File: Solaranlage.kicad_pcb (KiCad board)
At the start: 2 copper layers, 180.3 x 85 mm, 111 parts, among them J1 Screw_Terminal_01x02, J2 Screw_Terminal_01x02, J3 AVR-JTAG-10, J4 USB_B, J5 USB_B, J6 Screw_Terminal_01x02, J7 Screw_Terminal_01x02, Q1 2N3904, SW1 Rotary_Encoder_Switch_Panason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, SW2 100SP1T1B4M2QE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

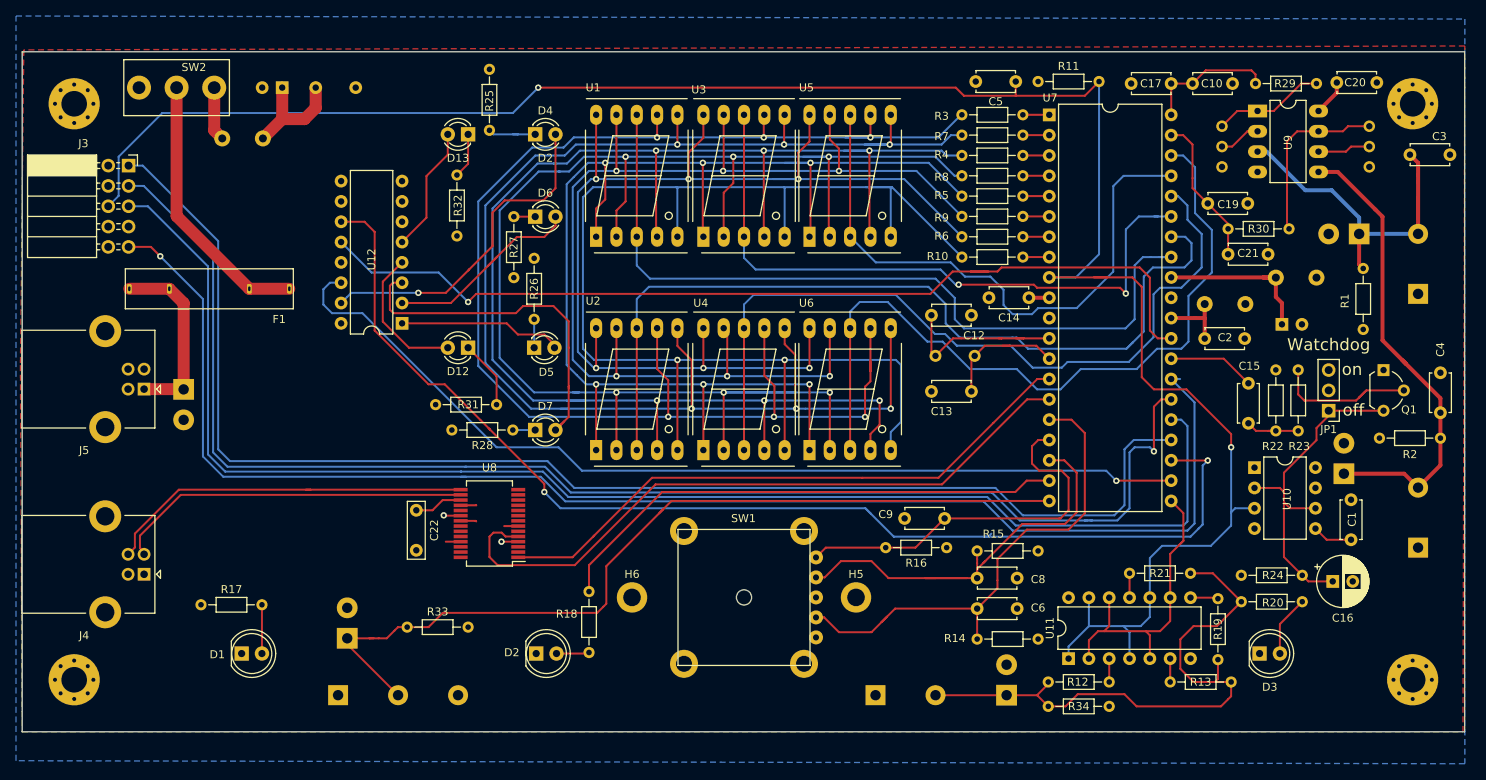
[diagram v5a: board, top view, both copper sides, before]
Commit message: created BOM; added ordering codes; changes some footprints; etc.
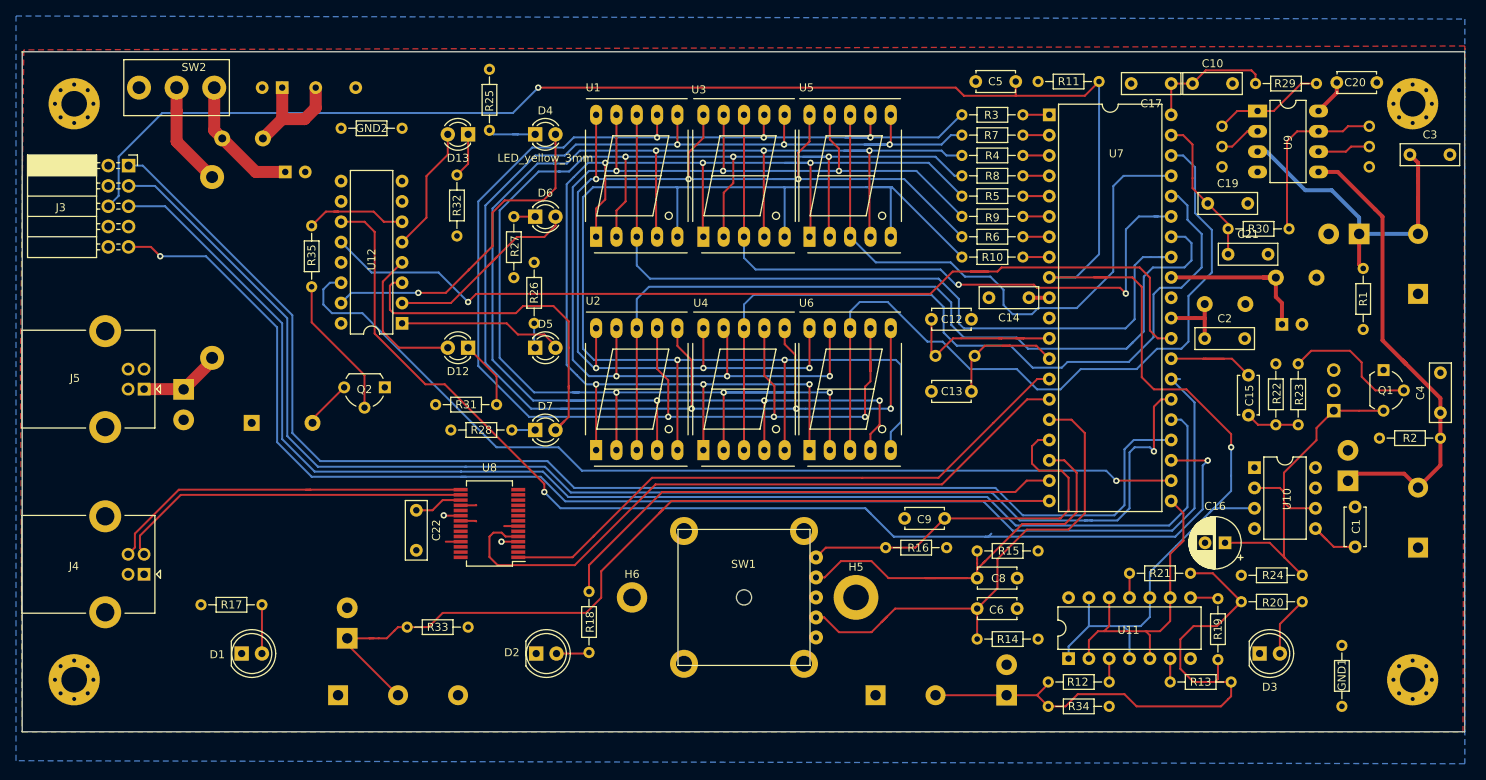
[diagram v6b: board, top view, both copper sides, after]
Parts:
- added BZ1: AL-60SP05/HT, Buzzer_Beeper:Buzzer_12x9.5RM7.6, B.Cu at (77.5, 101.6)
- added C23: 10uF, Capacitor_THT:CP_Radial_D6.3mm_P2.50mm, B.Cu at (81.7, 70.2)
- added GND1: 0, Resistor_THT:R_Axial_DIN0204_L3.6mm_D1.6mm_P7.62mm_Horizontal, F.Cu at (213.7, 129.4)
- added GND2: 0, Resistor_THT:R_Axial_DIN0204_L3.6mm_D1.6mm_P7.62mm_Horizontal, F.Cu at (88.6, 64.8)
- added Q2: 2N3904, Package_TO_SOT_THT:TO-92L_Wide, F.Cu at (94.1, 97.2)
- added R35: 1k, Resistor_THT:R_Axial_DIN0204_L3.6mm_D1.6mm_P7.62mm_Horizontal, F.Cu at (85.0, 84.6)
- C10, C14, C17, C19, C2, C21, C3, C4: footprint Capacitor_THT:C_Disc_D4.7mm_W2.5mm_P5.00mm -> Capacitor_THT:C_Rect_L7.2mm_W2.5mm_P5.00mm_FKS2_FKP2_MKS2_MKP2
- C11, C16, C18: value 13uF -> 10uF
- C22, C7: footprint Capacitor_THT:C_Rect_L7.0mm_W2.0mm_P5.00mm -> Capacitor_THT:C_Rect_L7.2mm_W2.5mm_P5.00mm_FKS2_FKP2_MKS2_MKP2
- D1: value LED_rot -> LED_red_5mm
- D12: value K -> LED_yellow_3mm
- D13: value M -> LED_yellow_3mm
- D2, D3: value LED_gruen -> LED_green_5mm
- D4: value D2 -> LED_yellow_3mm
- D5: value D1 -> LED_yellow_3mm
- D6: value TK -> LED_yellow_3mm
- D7: value TD -> LED_yellow_3mm
- F1: footprint fuse:5x20mm -> fuse:696101000002; moved to B.Cu
- H5: footprint MountingHole:MountingHole_2.2mm_M2_DIN965_Pad -> MountingHole:MountingHole_3.2mm_M3_DIN965_Pad
- JP1: moved to B.Cu
- moved C16 14.3 mm to (199.1, 116.6), turned to 180 degrees
- moved F1 10.0 mm to (72.5, 82.2), turned to 270 degrees
- moved C1 1.02 mm to (215.4, 117.1)
- moved D9 1.02 mm to (214.5, 108.8)
- moved C15 1.02 mm to (202.1, 95.6)
- moved R22 0.76 mm to (205.5, 101.8)
- moved R23 0.76 mm to (208.3, 101.8)
- moved JP1 0.63 mm to (212.7, 100.1), turned to 0 degrees
- moved C12 0.51 mm to (162.4, 88.6)
- moved R26 0.51 mm to (112.8, 89.2)
- moved D5 0.13 mm to (112.9, 92.2)
- moved R28 0.13 mm to (110.0, 102.5)
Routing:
- net Net-(F1-Pad1): track 33.9 -> 13.0 mm
- net Net-(Q2-Pad2): track 0.00 -> 17.8 mm
- net Net-(R35-Pad2): track 0.00 -> 13.1 mm
- net Net-(D10-Pad1): track 23.3 -> 10.4 mm
- net Net-(C23-Pad1): track 6.77 -> 16.4 mm
- net TCK: track 171.6 -> 164.9 mm
- net TMS: track 177.2 -> 170.9 mm
- net Net-(BZ1-Pad2): track 0.00 -> 6.08 mm
- net TDO: track 176.9 -> 171.1 mm
- net TDI: track 181.2 -> 176.6 mm
- net Net-(C16-Pad1): track 42.6 -> 46.7 mm
- net Net-(C1-Pad1): track 5.02 -> 7.88 mm
- net WDI: track 10.9 -> 13.0 mm
- net /KZ: track 99.0 -> 100.9 mm
- net Net-(Q1-Pad2): track 18.2 -> 17.0 mm
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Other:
- rule trace_min: 0.15 -> 0.2
- board text added: "500 mA"

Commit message: Production state Rev.B
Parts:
- C1, C15, C20, C5, C6, C8, C9: footprint Capacitor_THT:C_Disc_D4.7mm_W2.5mm_P5.00mm -> Capacitor_THT:C_Rect_L7.2mm_W2.5mm_P5.00mm_FKS2_FKP2_MKS2_MKP2
- moved J3 2.83 mm to (62.1, 72.3)
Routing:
- net \RST: track 257.9 -> 261.1 mm
- net TDI: track 176.6 -> 175.4 mm
- net TCK: track 164.9 -> 163.8 mm
- net TMS: track 170.9 -> 169.7 mm
- net TDO: track 171.1 -> 170.0 mm
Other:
- board text added: "Steuerung Solaranlage Rev. B (2021)"

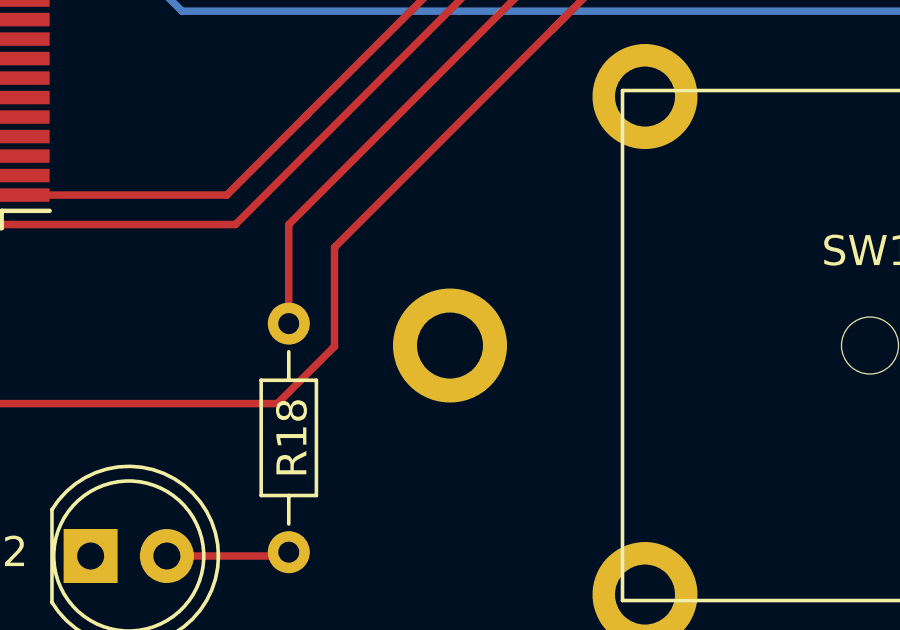
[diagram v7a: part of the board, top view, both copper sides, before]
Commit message: fixes after receiving RevB PCBs: - increased diameter of H6 to 3.2mm; -decrease radius of hole for encoder to 6.5mm
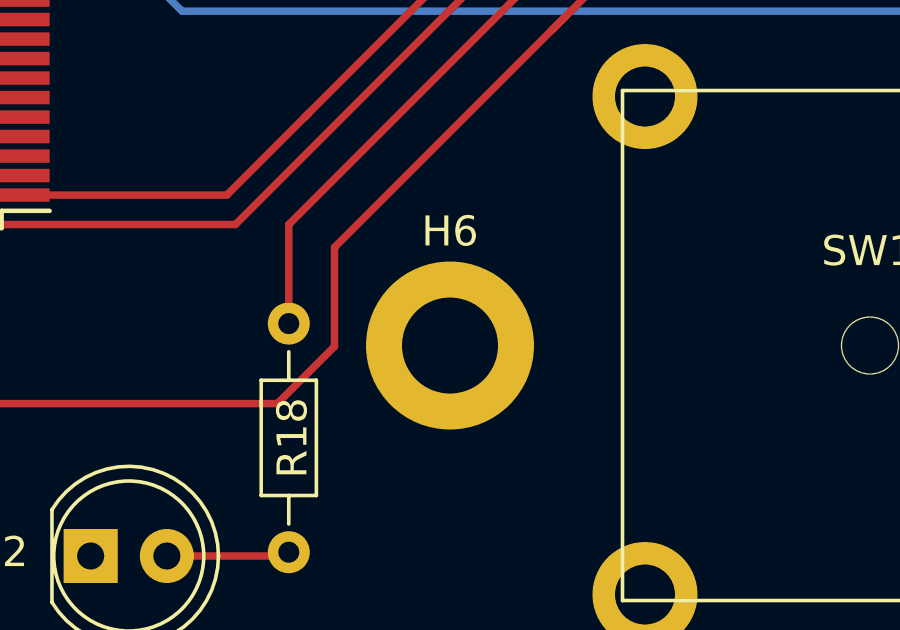
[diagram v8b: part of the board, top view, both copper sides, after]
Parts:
- H6: footprint MountingHole:MountingHole_2.2mm_M2_DIN965_Pad -> MountingHole:MountingHole_3.2mm_M3_DIN965_Pad
- J7: value Screw_Terminal_01x02 -> Screw_Terminal_01x03
- MECH1, MECH2: value Socket for NE555 (U10) -> 8 pin ic socket
- MECH3: value Socket for buffer (U11) -> 16 pin ic socket
- MECH4: value Socket shift register (U12) -> 16 pin ic socket
- MECH5: value Socket for ATMega32 (U7) -> 40 pin ic socket
